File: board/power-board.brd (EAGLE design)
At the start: 95.9 x 90.2 mm, 443 parts, among them J1 H1, J2 H2, J6 DF13-8P-1.25DS, J7 DF13-10P-1.25DS, J8 DF13-4P-1.25DS, J9 DF13-4P-1.25DS, Q3 SI7288, U1 INA214DCK, U10 INA214DCK, U11 INA214DCK, U12 INA214DCK, U13 MCP6561T-E/LT, U14 INA214DCK, U15 SN74AUP1G00DCK, U16 SN74LVC1G373DCK, U17 NTHD4508NT1, U18 MCP6561T-E/LT, U19 INA214DCK, U2 INA214DCK, U20 SN74AUP1G00DCK, U21 SN74LVC1G373DCK, U22 NTHD4508NT1, U23 MCP6561T-E/LT, U24 INA214DCK, U25 SN74AUP1G00DCK, U26 SN74LVC1G373DCK, U27 NTHD4508NT1, U28 MCP6561T-E/LT, U29 INA214DCK, U3 INA214DCK, U30 SN74AUP1G00DCK, U31 SN74LVC1G373DCK, U32 NTHD4508NT1, U33 MCP6561T-E/LT, U34 INA214DCK, U35 SN74AUP1G00DCK, U36 SN74LVC1G373DCK, U37 NTHD4508NT1, U38 MCP6561T-E/LT, U39 INA214DCK, U4 INA214DCK, U40 SN74AUP1T08DCK, U41 SN74LVC1G373DCK, U42 FDS8858CZ, U43 TLV3491AIDBV, U44 TPS62132RGT, U45 FDS8858CZ, U46 TLV3491AIDBV, U47 TPS62133RGT, U48 FDS8858CZ, U49 MSP430F2132, U5 INA214DCK, U50 ADG732, U51 SPV1040T, U52 SPV1040T, U53 BQ24650_RVA_16, U54 INA214DCK, U55 SPV1040T, U56 SPV1040T, U57 SPV1040T, U58 SPV1040T, U6 INA214DCK, U7 INA214DCK, U8 INA214DCK, U9 INA214DCK, X1 32.768k

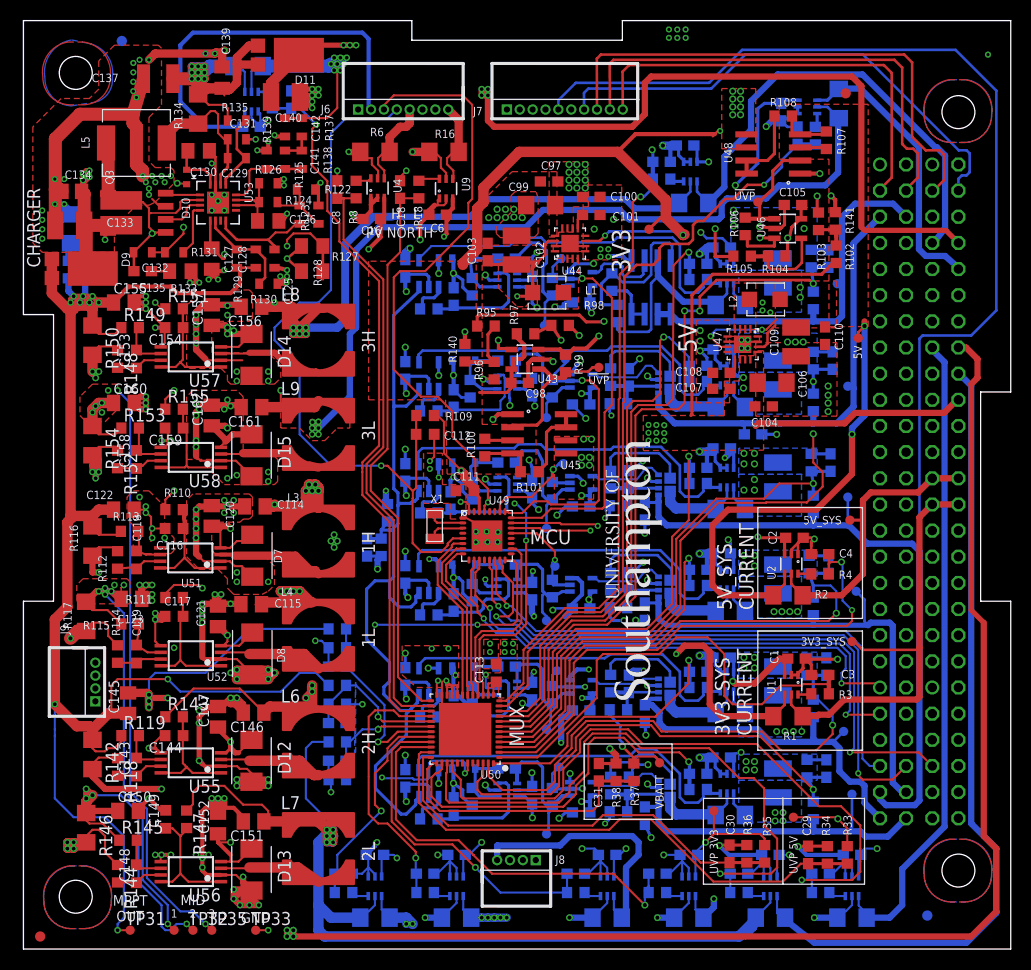
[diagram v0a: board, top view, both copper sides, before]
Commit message: separating vbat/charge. routing improvements for 3.3/5V regs
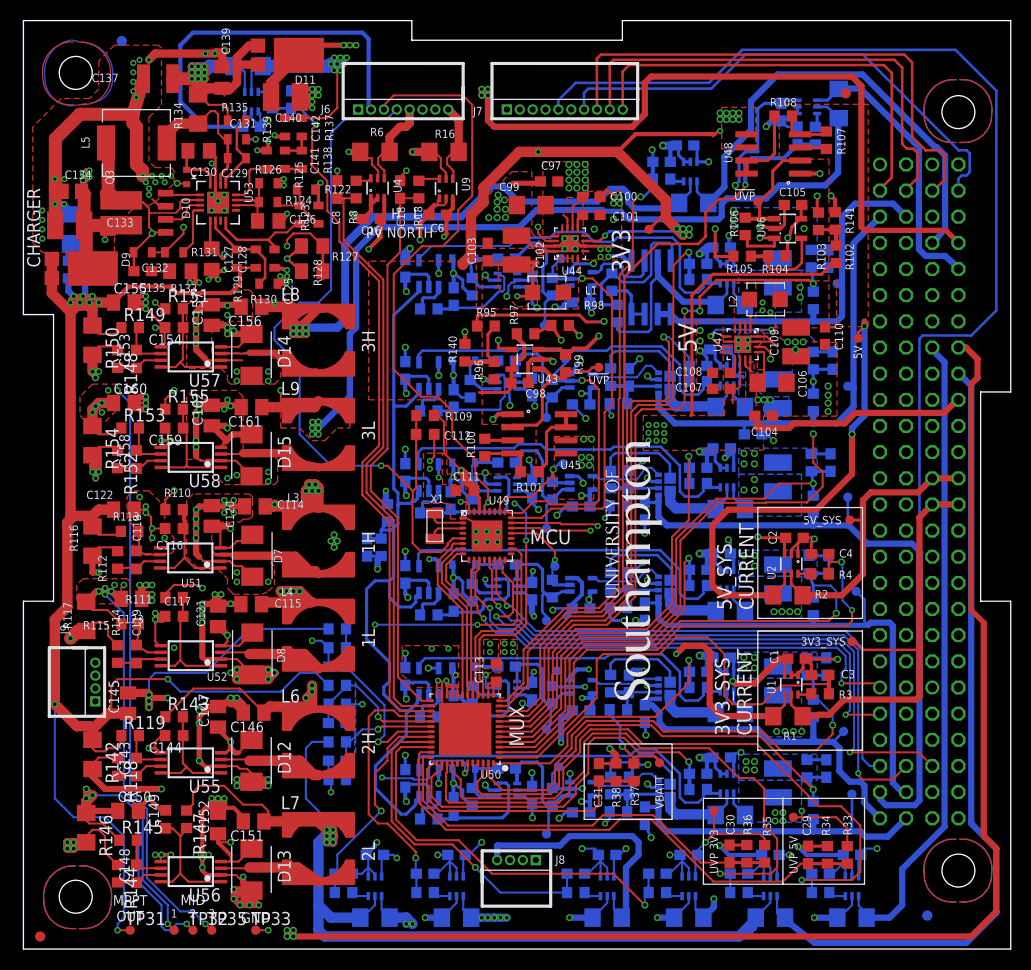
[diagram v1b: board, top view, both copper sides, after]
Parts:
- moved C84 1.83 mm to (73.3, 53.9)
- moved C104 0.91 mm to (71.9, 51.8)
- moved C99 0.91 mm to (49.3, 72.2)
- moved C78 0.30 mm to (67.5, 58.2)
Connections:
- new net CHARGE_BATT: C142.1, J2.41, J2.42, J2.43, J2.44, R132.2, R137.2, U54.5
- net VBATT: no longer C142.1, J2.41, J2.42, J2.43, J2.44, R132.2, R137.2, U54.5
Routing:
- net VBATT: track 106.7 -> 141.1 mm, vias 45 -> 30
- net CHARGE_BATT: track 0.00 -> 25.2 mm, vias 0 -> 8
- net GND: track 500.0 -> 521.8 mm, vias 256 -> 265
- net REG3V3: track 164.9 -> 171.7 mm, vias 6 -> 12
- net UVP3V3_OUT: track 284.0 -> 281.0 mm, vias 57 -> 58
- net N$4: track 0.00 -> 2.94 mm
- net MPPT3H_PV_P: track 77.4 -> 79.9 mm
- net REG5V: track 62.1 -> 63.6 mm, vias 4 -> 5
- net N$78: track 11.5 -> 10.3 mm
- net PV_TOP2_CSENSE_MUX: track 74.8 -> 75.9 mm
- net OCP5_CSENSE_MUX: track 53.6 -> 54.7 mm
- net CHARGE_IN: track 230.6 -> 229.7 mm
- net UVP5V_OUT: track 15.1 -> 15.7 mm
- added copper zone on layer 2, net CHARGE_BATT
- added copper zone on layer 2, net REG3V3

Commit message: updating component values
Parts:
- R102, R95: value 1.5k -> 1.45k
- R103, R96: value 1k -> 1.02k
- R104: value 1.24 -> 1.24k
- R106, R99: value 15k -> 10k
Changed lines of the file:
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@@
 <attribute name="NAME" x="48.7553" y="53.5559" size="0.8128" layer="25" ratio="14"/>
 </element>
-<element name="R95" library="rcl" package="R0603" value="1.5k" x="44.9199" y="60.5028" smashed="yes">
+<element name="R95" library="rcl" package="R0603" value="1.45k" x="44.9199" y="60.5028" smashed="yes">
 <attribute name="NAME" x="43.9801" y="61.4426" size="0.8128" layer="25" ratio="14"/>
 </element>
-<element name="R96" library="rcl" package="R0603" value="1k" x="45.72" y="56.1721" smashed="yes" rot="R90">
+<element name="R96" library="rcl" package="R0603" value="1.02k" x="45.72" y="56.1721" smashed="yes" rot="R90">
 <attribute name="NAME" x="43.815" y="57.2389" size="0.8128" layer="25" ratio="14" rot="R270"/>
 </element>
@@
 <attribute name="NAME" x="48.0441" y="60.6298" size="0.8128" layer="25" ratio="14" rot="R90"/>
 </element>
-<element name="R99" library="rcl" package="R0603" value="15k" x="52.6415" y="56.8706" smashed="yes" rot="R270">
+<element name="R99" library="rcl" package="R0603" value="10k" x="52.6415" y="56.8706" smashed="yes" rot="R270">
 <attribute name="NAME" x="54.3179" y="55.7784" size="0.8128" layer="25" ratio="14" rot="R90"/>
 </element>
@@
 <attribute name="NAME" x="73.3933" y="73.1139" size="0.8128" layer="25" ratio="14"/>
 </element>
-<element name="R102" library="rcl" package="R0603" value="1.5k" x="78.9432" y="67.4751" smashed="yes" rot="R90">
+<element name="R102" library="rcl" package="R0603" value="1.45k" x="78.9432" y="67.4751" smashed="yes" rot="R90">
 <attribute name="NAME" x="80.645" y="65.9257" size="0.8128" layer="25" ratio="14" rot="R90"/>
 </element>
-<element name="R103" library="rcl" package="R0603" value="1k" x="77.216" y="70.6755" smashed="yes" rot="R270">
+<element name="R103" library="rcl" package="R0603" value="1.02k" x="77.216" y="70.6755" smashed="yes" rot="R270">
 <attribute name="NAME" x="77.9018" y="65.9511" size="0.8128" layer="25" ratio="14" rot="R90"/>
 </element>
@@
 <attribute name="NAME" x="68.2498" y="65.6717" size="0.8128" layer="25" ratio="14"/>
 </element>
-<element name="R104" library="rcl" package="R0603" value="1.24" x="73.152" y="67.2973" smashed="yes">
+<element name="R104" library="rcl" package="R0603" value="1.24k" x="73.152" y="67.2973" smashed="yes">
 <attribute name="NAME" x="71.7042" y="65.6463" size="0.8128" layer="25" ratio="14"/>
 </element>
-<element name="R106" library="rcl" package="R0603" value="15k" x="70.0913" y="70.1802" smashed="yes" rot="R90">
+<element name="R106" library="rcl" package="R0603" value="10k" x="70.0913" y="70.1802" smashed="yes" rot="R90">
 <attribute name="NAME" x="68.6181" y="71.7804" size="0.8128" layer="25" ratio="14" rot="R270"/>
 </element>

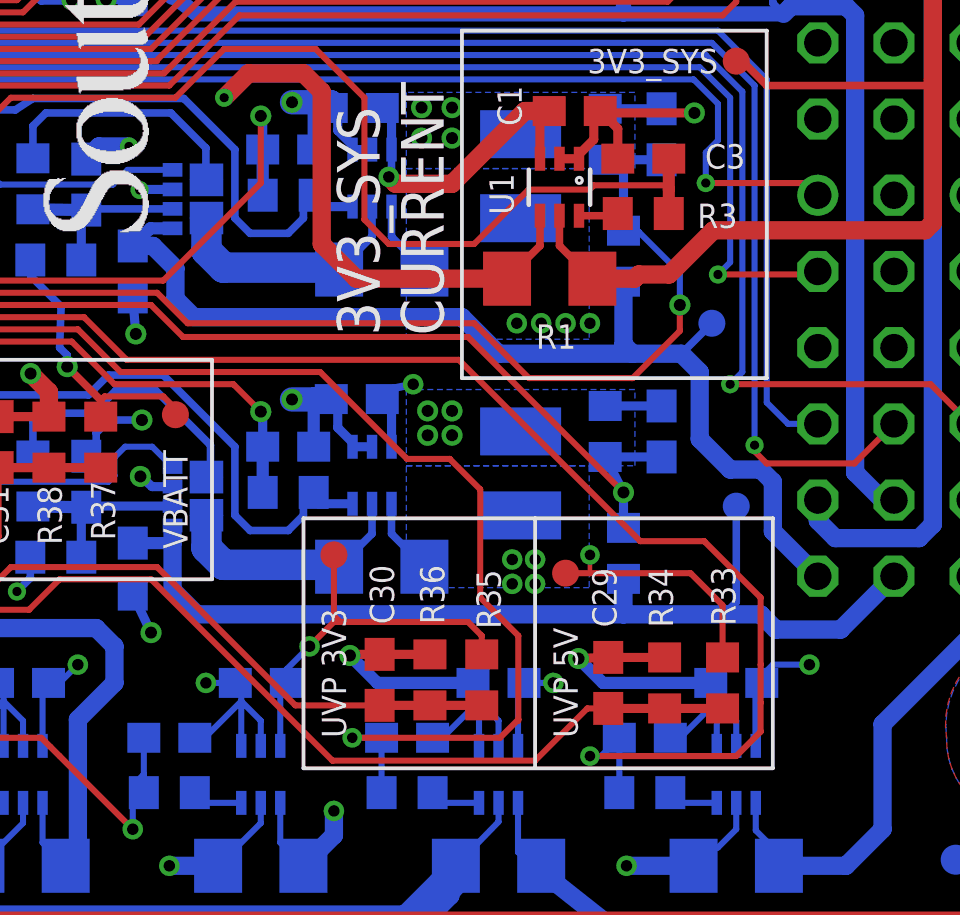
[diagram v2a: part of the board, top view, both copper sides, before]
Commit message: adding i2c pullups
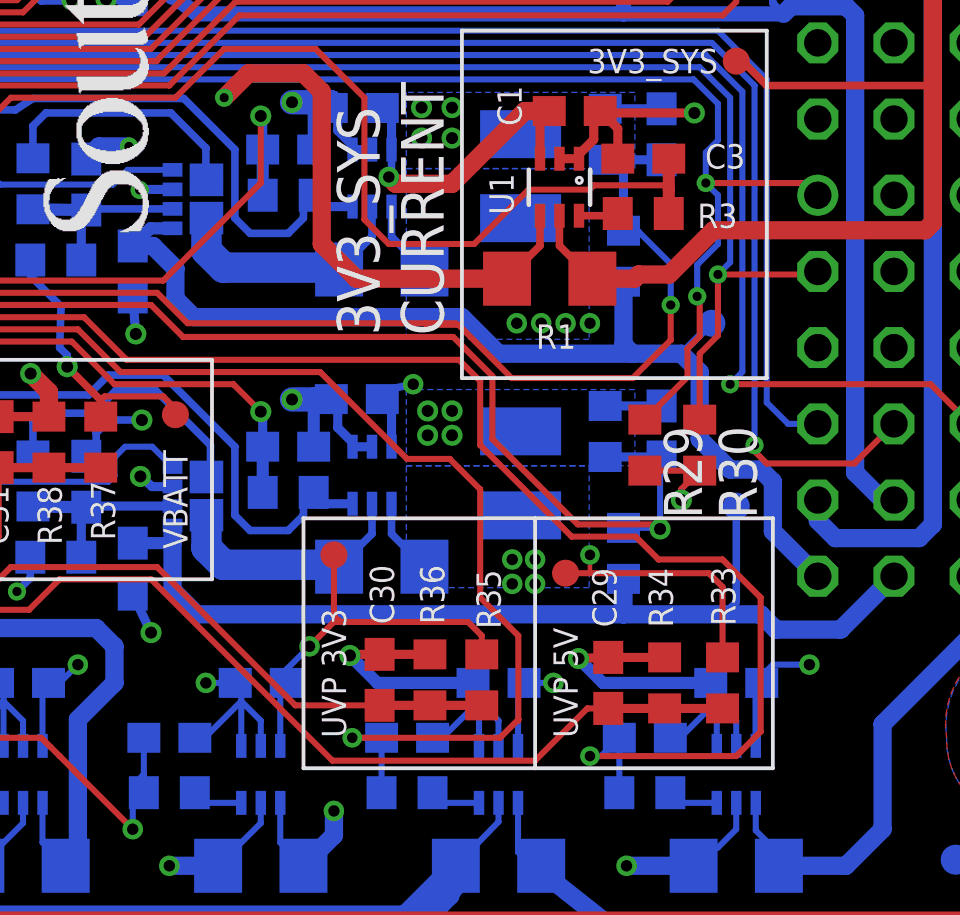
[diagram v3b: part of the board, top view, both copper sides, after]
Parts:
- added R29, R30: 4k7, rcl:R0603
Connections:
- net BATT_I2C_SCL: now also R30.1
- net BATT_I2C_SDA: now also R29.1
- net UVP3V3_OUT: now also R29.2, R30.2
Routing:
- net UVP3V3_OUT: track 281.0 -> 295.6 mm, vias 58 -> 59
- net BATT_I2C_SDA: track 49.8 -> 58.9 mm, vias 2 -> 3
- net BATT_I2C_SCL: track 52.5 -> 57.6 mm
- net OCP1_VSENSE: track 47.2 -> 51.3 mm
- net PV_EAST1_CSENSE_MUX: track 64.6 -> 65.8 mm
- net OCP2_VSENSE: track 50.2 -> 51.0 mm

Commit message: fixing silk layer
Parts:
- moved C87 0.25 mm to (36.8, 66.1)
- moved C96 0.25 mm to (33.1, 39.0)
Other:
- board text added: "Rev 1.2 Nov' 18"
- board text added: "UoS3 Power Supply Tom Gillbe Adrian Wheeldon Reece Williams James Boyle Josh Oldfield Matt Brejza"
- board text removed: "MPPT1_PV_P"
- board text removed: "Rev 1.1 Mar'17"
- board text removed: "UoS3 Power Supply Tom Gillbe Adrian Wheeldon Reece Williams James Boyle Josh Oldfield"

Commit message: updated UVP componets to 7.2V/8V to match changes to the previous board. Also increased the UVP components by 10x to reduce current consumption
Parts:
- R102, R95: value 1.45k -> 20k
- R103, R96: value 1.02k -> 10.2k
- R104, R97: value 1.24k -> 12.4k
- R105, R98: value 12.4k -> 124k
- R106, R99: value 10k -> 100k
- R140, R141: value 402 -> 4.02k
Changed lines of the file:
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@@
 <?xml version="1.0" encoding="utf-8"?>
 <!DOCTYPE eagle SYSTEM "eagle.dtd">
-<eagle version="9.0.1">
+<eagle version="6.6.0">
 <drawing>
 <settings>
 <setting alwaysvectorfont="no"/>
-<setting keepoldvectorfont="yes"/>
 <setting verticaltext="up"/>
 </settings>
@@
 <text x="79.248" y="85.344" size="1.4224" layer="22" font="vector" ratio="12" rot="MR0">T2C</text>
 <wire x1="78.6384" y1="9.9568" x2="78.6384" y2="9.906" width="0.127" layer="22"/>
-<wire x1="90.8304" y1="0" x2="90.8304" y2="11.3792" width="0.127" layer="22"/>
 <text x="62.1792" y="13.6144" size="0.8128" layer="21" font="vector" ratio="12" rot="R90">VBATT</text>
 <wire x1="54.4576" y1="12.5984" x2="62.992" y2="12.5984" width="0.127" layer="21"/>
@@
 <param name="dpMaxLengthDifference" value="10mm"/>
 <param name="dpGapFactor" value="2.5"/>
+<param name="checkGrid" value="0"/>
 <param name="checkAngle" value="0"/>
 <param name="checkFont" value="1"/>
 <param name="checkRestrict" value="1"/>
-<param name="checkStop" value="0"/>
-<param name="checkValues" value="0"/>
 <param name="useDiameter" value="13"/>
 <param name="maxErrors" value="50"/>
@@
 <pass name="Default">
 <param name="RoutingGrid" value="6.25mil"/>
-<param name="AutoGrid" value="1"/>
-<param name="Efforts" value="0"/>
-<param name="TopRouterVariant" value="1"/>
 <param name="tpViaShape" value="round"/>
 <param name="PrefDir.1" value="*"/>
@@
 <attribute name="NAME" x="47.1297" y="53.2003" size="0.8128" layer="25" font="vector" ratio="14"/>
 </element>
-<element name="R95" library="rcl" package="R0603" value="1.45k" x="44.9199" y="60.5028" smashed="yes">
+<element name="R95" library="rcl" package="R0603" value="20k" x="44.9199" y="60.5028" smashed="yes">
 <attribute name="NAME" x="43.9801" y="61.4426" size="0.8128" layer="25" font="vector" ratio="14"/>
 </element>
-<element name="R96" library="rcl" package="R0603" value="1.02k" x="45.72" y="56.1721" smashed="yes" rot="R90">
+<element name="R96" library="rcl" package="R0603" value="10.2k" x="45.72" y="56.1721" smashed="yes" rot="R90">
 <attribute name="NAME" x="44.0182" y="57.2389" size="0.8128" layer="25" font="vector" ratio="14" rot="R270"/>
 </element>
-<element name="R98" library="rcl" package="R0603" value="12.4k" x="52.1208" y="60.5663" smashed="yes" rot="R180">
+<element name="R98" library="rcl" package="R0603" value="124k" x="52.1208" y="60.5663" smashed="yes" rot="R180">
 <attribute name="NAME" x="51.2826" y="58.9153" size="0.8128" layer="25" font="vector" ratio="14"/>
 </element>
-<element name="R97" library="rcl" package="R0603" value="1.24k" x="48.768" y="59.7535" smashed="yes" rot="R180">
+<element name="R97" library="rcl" package="R0603" value="12.4k" x="48.768" y="59.7535" smashed="yes" rot="R180">
 <attribute name="NAME" x="49.8094" y="61.4045" size="0.8128" layer="25" font="vector" ratio="14" rot="R180"/>
 </element>
-<element name="R99" library="rcl" package="R0603" value="10k" x="52.6415" y="56.8706" smashed="yes" rot="R270">
+<element name="R99" library="rcl" package="R0603" value="100k" x="52.6415" y="56.8706" smashed="yes" rot="R270">
 <attribute name="NAME" x="54.3179" y="55.7784" size="0.8128" layer="25" font="vector" ratio="14" rot="R90"/>
 </element>
@@
 <attribute name="NAME" x="73.3933" y="73.1139" size="0.8128" layer="25" font="vector" ratio="14"/>
 </element>
-<element name="R102" library="rcl" package="R0603" value="1.45k" x="78.9432" y="67.4751" smashed="yes" rot="R90">
+<element name="R102" library="rcl" package="R0603" value="20k" x="78.9432" y="67.4751" smashed="yes" rot="R90">
 <attribute name="NAME" x="80.645" y="65.9257" size="0.8128" layer="25" font="vector" ratio="14" rot="R90"/>
 </element>
-<element name="R103" library="rcl" package="R0603" value="1.02k" x="77.216" y="70.6755" smashed="yes" rot="R270">
+<element name="R103" library="rcl" package="R0603" value="10.2k" x="77.216" y="70.6755" smashed="yes" rot="R270">
 <attribute name="NAME" x="77.9018" y="65.9511" size="0.8128" layer="25" font="vector" ratio="14" rot="R90"/>
 </element>
-<element name="R105" library="rcl" package="R0603" value="12.4k" x="69.7992" y="67.2973" smashed="yes">
+<element name="R105" library="rcl" package="R0603" value="124k" x="69.7992" y="67.2973" smashed="yes">
 <attribute name="NAME" x="68.2498" y="65.6717" size="0.8128" layer="25" font="vector" ratio="14"/>
 </element>
-<element name="R104" library="rcl" package="R0603" value="1.24k" x="73.152" y="67.2973" smashed="yes">
+<element name="R104" library="rcl" package="R0603" value="12.4k" x="73.152" y="67.2973" smashed="yes">
 <attribute name="NAME" x="71.7042" y="65.6463" size="0.8128" layer="25" font="vector" ratio="14"/>
 </element>
-<element name="R106" library="rcl" package="R0603" value="10k" x="70.0913" y="70.1802" smashed="yes" rot="R90">
+<element name="R106" library="rcl" package="R0603" value="100k" x="70.0913" y="70.1802" smashed="yes" rot="R90">
 <attribute name="NAME" x="68.6181" y="71.7804" size="0.8128" layer="25" font="vector" ratio="14" rot="R270"/>
 </element>
@@
 <attribute name="NAME" x="26.289" y="80.6958" size="0.8128" layer="26" font="vector" ratio="14" rot="MR270"/>
 </element>
-<element name="R140" library="rcl" package="R0603" value="402" x="42.8752" y="57.912" smashed="yes" rot="R90">
+<element name="R140" library="rcl" package="R0603" value="4.02k" x="42.8752" y="57.912" smashed="yes" rot="R90">
 <attribute name="NAME" x="41.275" y="59.563" size="0.8128" layer="25" font="vector" ratio="14" rot="R270"/>
 </element>
-<element name="R141" library="rcl" package="R0603" value="402" x="78.8416" y="70.7136" smashed="yes" rot="R90">
+<element name="R141" library="rcl" package="R0603" value="4.02k" x="78.8416" y="70.7136" smashed="yes" rot="R90">
 <attribute name="NAME" x="80.645" y="69.469" size="0.8128" layer="25" font="vector" ratio="14" rot="R90"/>
 </element>
